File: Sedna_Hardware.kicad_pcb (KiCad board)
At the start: 2 copper layers, 50 parts, among them J1 PJ-102A, J10 5-103634-2, J11 2-644488-2, J2 61201021721, J3 PPTC141LFBN-RC, J4 0878340619, J5 2-644803-3, J6 2-644488-3, J7 1935161, J8 1935161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

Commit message: Quick touch ups
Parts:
- moved C5 5.08 mm to (141.2, 91.9), turned to -90 degrees
- moved R1 3.56 mm to (167.1, 85.3)
- moved D1 2.29 mm to (178.8, 85.3)
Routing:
- net +3V3: track 259.7 -> 257.3 mm
- net +5V: track 105.2 -> 103.3 mm
- net Net-(D1-Pad1): track 2.79 -> 4.06 mm
- added copper zone on B.Cu, net GND
- added copper zone on F.Cu, net GND
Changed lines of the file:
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@@
   )
   (footprint "Capacitor_THT:C_Disc_D9.0mm_W5.0mm_P5.00mm" (layer "F.Cu")
-    (at 141.229 97.028 90)
+    (at 141.224 91.948 -90)
     (descr "C, Disc series, Radial, pin pitch=5.00mm, , diameter*width=9*5.0mm^2, Capacitor, http://www.vishay.com/docs/28535/vy2series.pdf")
     (tags "C Disc series Radial pin pitch 5.00mm  diameter 9mm width 5.0mm Capacitor")
@@
     (fp_line (start 7 -2.5) (end -2 -2.5) (layer "F.Fab") (width 0.1))
     (fp_line (start 7 2.5) (end 7 -2.5) (layer "F.Fab") (width 0.1))
-    (pad "1" thru_hole circle (at 0 0 90) (size 2 2) (drill 1) (layers *.Cu *.Mask)
+    (pad "1" thru_hole circle (at 0 0 270) (size 2 2) (drill 1) (layers *.Cu *.Mask)
       (net 2 "GND") (pintype "passive"))
-    (pad "2" thru_hole circle (at 5 0 90) (size 2 2) (drill 1) (layers *.Cu *.Mask)
+    (pad "2" thru_hole circle (at 5 0 270) (size 2 2) (drill 1) (layers *.Cu *.Mask)
       (net 3 "+3V3") (pintype "passive"))
     (model "${KICAD6_3DMODEL_DIR}/Capacitor_THT.3dshapes/C_Disc_D9.0mm_W5.0mm_P5.00mm.wrl"
@@
   )
   (footprint "digikey-footprints:LED_3mm_Radial" (layer "F.Cu")
-    (at 181.107 85.344)
+    (at 178.816 85.344)
     (descr "http://optoelectronics.liteon.com/upload/download/DS20-2000-343/1CHKxKNN.pdf")
     (property "Category" "Optoelectronics")
@@
   )
   (footprint "Resistor_THT:R_Axial_DIN0204_L3.6mm_D1.6mm_P5.08mm_Horizontal" (layer "F.Cu")
-    (at 170.693 85.344)
+    (at 167.132 85.344)
     (descr "Resistor, Axial_DIN0204 series, Axial, Horizontal, pin pitch=5.08mm, 0.167W, length*diameter=3.6*1.6mm^2, http://cdn-reichelt.de/documents/datenblatt/B400/1_4W%23YAG.pdf")
     (tags "Resistor Axial_DIN0204 series Axial Horizontal pin pitch 5.08mm 0.167W length 3.6mm diameter 1.6mm")
@@
     )
   )
-  (gr_line (start 101.092 148.336) (end 101.092 54.356) (layer "B.Cu") (width 0.2))
   (gr_line (start 186.436 54.356) (end 186.436 148.336) (layer "B.Cu") (width 0.2))
   (gr_line (start 186.436 148.336) (end 101.092 148.336) (layer "B.Cu") (width 0.2))
   (gr_line (start 101.092 54.356) (end 186.436 54.356) (layer "B.Cu") (width 0.2))
+  (gr_line (start 101.092 148.336) (end 101.092 54.356) (layer "B.Cu") (width 0.2))
   (gr_line (start 117.584238 133.604) (end 192.768238 133.604) (layer "F.CrtYd") (width 0.05))
   (gr_line (start 115.824 67.056) (end 115.824 54.356) (layer "User.2") (width 0.15))
@@
   (gr_line (start 175.26 54.356) (end 175.26 147.828) (layer "User.3") (width 0.15))
   (gr_line (start 175.26 147.828) (end 120.904 147.828) (layer "User.3") (width 0.15))
-  (gr_line (start 182.885 57.404) (end 103.129 57.404) (layer "User.4") (width 0.15))
-  (gr_line (start 103.129 57.404) (end 103.383 146.812) (layer "User.4") (width 0.15))
-  (gr_line (start 103.383 146.812) (end 183.139 146.812) (layer "User.4") (width 0.15))
-  (gr_line (start 183.139 146.812) (end 182.885 57.404) (layer "User.4") (width 0.15))
+  (gr_line (start 183.139004 56.388) (end 102.616 56.388) (layer "User.4") (width 0.15))
+  (gr_line (start 102.616 56.388) (end 102.616 146.812) (layer "User.4") (width 0.15))
+  (gr_line (start 102.616 146.812) (end 183.139004 146.812) (layer "User.4") (width 0.15))
+  (gr_line (start 183.139004 146.812) (end 183.139004 56.388) (layer "User.4") (width 0.15))
   (segment (start 163.601 89.448) (end 144.357 89.448) (width 1.016) (layer "F.Cu") (net 1))
   (segment (start 134.657004 84.511004) (end 132.498 82.352) (width 1.0668) (layer "F.Cu") (net 1))
   (segment (start 163.601 89.448) (end 165.274113 91.121113) (width 1.016) (layer "F.Cu") (net 1))
+  (segment (start 158.496 86.365004) (end 158.501004 86.36) (width 1.016) (layer "F.Cu") (net 1))
   (segment (start 156.075 82.685) (end 155.956 82.804) (width 0.762) (layer "F.Cu") (net 1))
   (segment (start 168.193 105.156) (end 164.683 105.156) (width 1.016) (layer "F.Cu") (net 1))
@@
   (segment (start 134.657004 86.36) (end 134.657004 84.511004) (width 1.0668) (layer "F.Cu") (net 1))
   (segment (start 155.956 82.804) (end 155.961 82.804) (width 1.016) (layer "F.Cu") (net 1))
-  (segment (start 161.589 89.448) (end 158.501 86.36) (width 1.016) (layer "F.Cu") (net 1))
   (segment (start 141.229 86.32) (end 135.452 86.32) (width 1.016) (layer "F.Cu") (net 1))
   (segment (start 170.693 91.629113) (end 170.693 102.656) (width 1.016) (layer "F.Cu") (net 1))
   (segment (start 163.581 89.428) (end 163.601 89.448) (width 0.4318) (layer "F.Cu") (net 1))
   (segment (start 170.185 91.121113) (end 174.461613 91.121113) (width 1.016) (layer "F.Cu") (net 1))
+  (segment (start 158.496 88.9) (end 158.496 86.365004) (width 1.016) (layer "F.Cu") (net 1))
   (segment (start 134.657 87.115) (end 134.625 87.083) (width 0.762) (layer "F.Cu") (net 1))
   (segment (start 134.697 87.075) (end 134.657 87.115) (width 0.25) (layer "F.Cu") (net 1))
@@
   (via (at 161.549 112.268) (size 1.27) (drill 0.889) (layers "F.Cu" "B.Cu") (net 3))
   (segment (start 157.017 124.46) (end 156.977 124.46) (width 0.25) (layer "B.Cu") (net 3))
+  (segment (start 167.132 87.371) (end 167.132 85.344) (width 0.762) (layer "B.Cu") (net 3))
   (segment (start 141.229 100.828) (end 141.224 100.833) (width 0.25) (layer "B.Cu") (net 3))
   (segment (start 154.437 127) (end 153.929 127.508) (width 0.762) (layer "B.Cu") (net 3))
   (segment (start 175.004 135.375) (end 175.004 135.8565) (width 0.4318) (layer "B.Cu") (net 3))
-  (segment (start 169.169 85.344) (end 170.693 85.344) (width 0.762) (layer "B.Cu") (net 3))
-  (segment (start 167.137 87.376) (end 169.169 85.344) (width 0.762) (layer "B.Cu") (net 3))
   (segment (start 168.6488 96.524145) (end 168.469222 96.524145) (width 0.762) (layer "B.Cu") (net 3))
   (segment (start 107.732789 125.718211) (end 107.732789 133.595789) (width 0.762) (layer "B.Cu") (net 3))
@@
   (segment (start 171.201 131.572) (end 175.004 135.375) (width 0.4318) (layer "B.Cu") (net 3))
   (segment (start 161.549 104.083) (end 161.549 112.268) (width 0.762) (layer "B.Cu") (net 3))
+  (segment (start 167.137 87.376) (end 167.132 87.371) (width 0.762) (layer "B.Cu") (net 3))
   (segment (start 167.09222 97.901147) (end 167.09222 101.87378) (width 0.762) (layer "B.Cu") (net 3))
   (segment (start 141.229 97.028) (end 123.957 97.028) (width 0.762) (layer "B.Cu") (net 3))
@@
   (segment (start 161.484 131.699) (end 161.611 131.572) (width 0.4318) (layer "F.Cu") (net 33))
   (segment (start 161.484 131.699) (end 161.93 131.699) (width 0.25) (layer "F.Cu") (net 33))
-  (segment (start 175.773 85.344) (end 178.567 85.344) (width 0.762) (layer "B.Cu") (net 34))
+  (segment (start 172.212 85.344) (end 176.276 85.344) (width 0.4318) (layer "B.Cu") (net 34))
   (segment (start 124.497004 90.512996) (end 124.332 90.678) (width 1.016) (layer "F.Cu") (net 35))
   (segment (start 124.497004 85.652996) (end 127.798 82.352) (width 1.016) (layer "F.Cu") (net 35))
@@
       )
     )
+  )
+  (zone (net 2) (net_name "GND") (layer "F.Cu") (hatch edge 0.508)
+    (connect_pads (clearance 0.508))
+    (min_thickness 0.254) (filled_areas_thickness no)
+    (fill (thermal_gap 0.508) (thermal_bridge_width 0.508))
+    (polygon
+      (pts
+        (xy 181.864 145.796)
+        (xy 103.632 145.796)
+        (xy 103.632 57.404)
+        (xy 181.864 57.404)
+      )
+    )
+  )
+  (zone (net 2) (net_name "GND") (layer "B.Cu") (hatch edge 0.508)
+    (connect_pads (clearance 0.508))
+    (min_thickness 0.254) (filled_areas_thickness no)
+    (fill (thermal_gap 0.508) (thermal_bridge_width 0.508))
+    (polygon
+      (pts
+        (xy 181.864 145.796)
+        (xy 103.632 145.796)
+        (xy 103.632 57.404)
+        (xy 181.864 57.404)
+      )
+    )

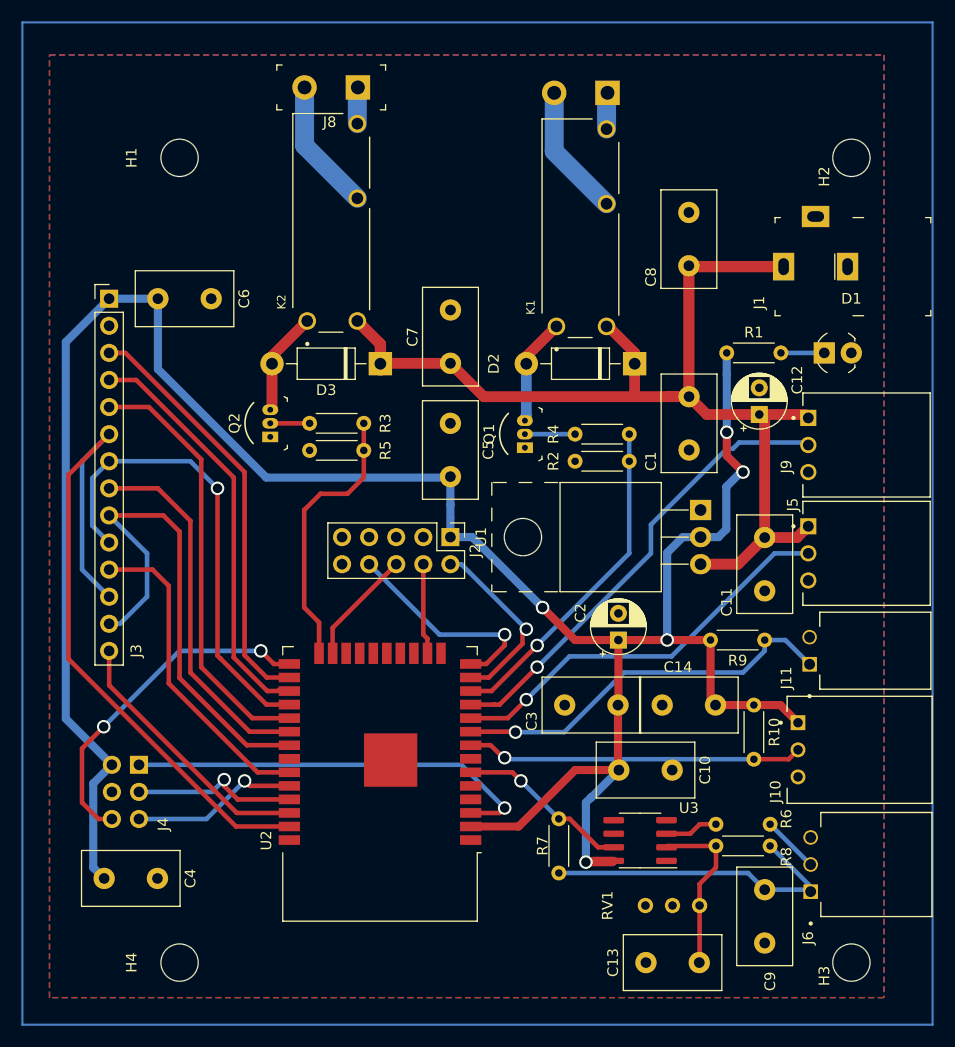
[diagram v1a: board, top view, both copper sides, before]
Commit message: placed potentiemeter and program header on the front side
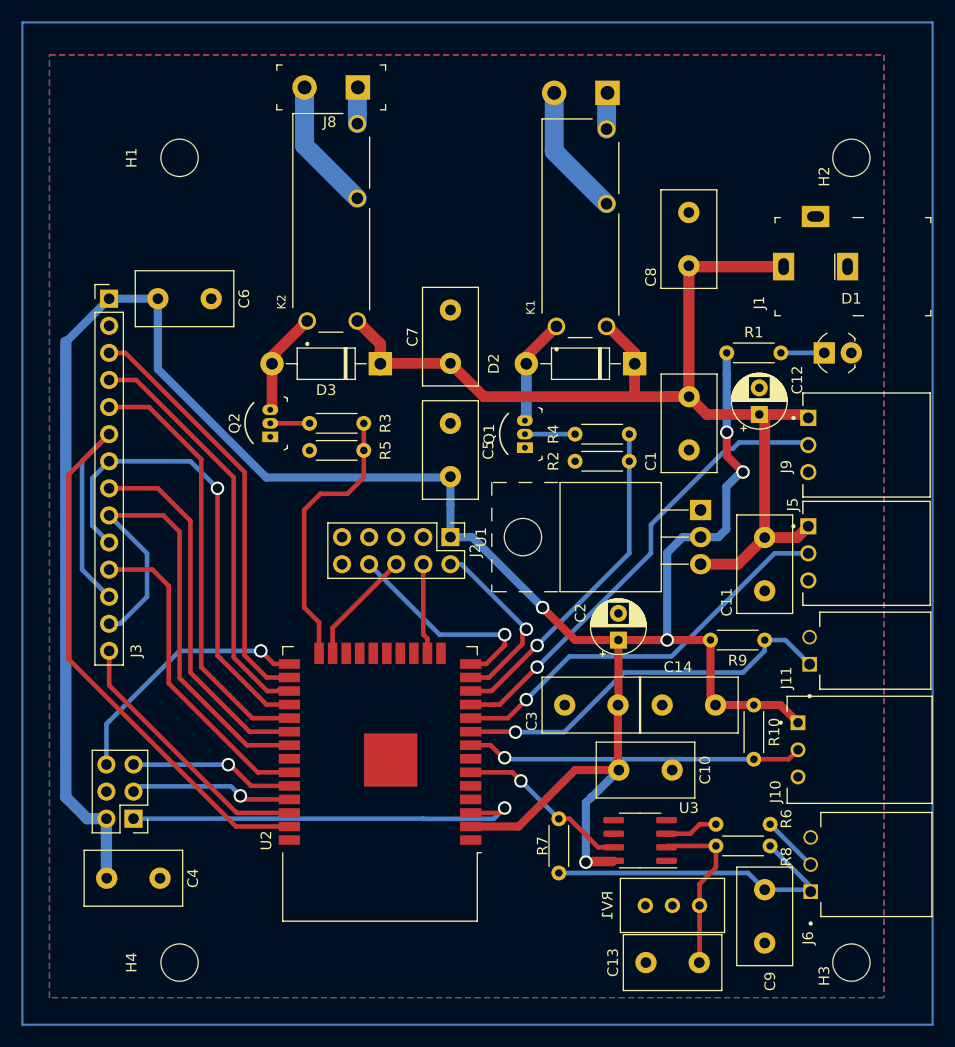
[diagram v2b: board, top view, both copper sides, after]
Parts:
- J4, RV1: moved to F.Cu
- moved J4 5.08 mm to (111.5, 129.0)
- moved C4 0.24 mm to (109.0, 134.6)
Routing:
- net PROG_IO0: track 33.2 -> 25.2 mm, vias 2 -> 1
- net PROG_EN: track 39.3 -> 38.6 mm
